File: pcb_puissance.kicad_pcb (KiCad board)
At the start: 2 copper layers, 126.5 x 120.5 mm, 40 parts, among them J1 1755736, J10 Conn_01x02, J11 Conn_01x02, J2 1755736, J3 1755736, J4 1755736, J5 1755736, J6 1755736, J7 1755736, J8 1755736, J9 Conn_01x02, K1 SRD-05VDC-SL-C

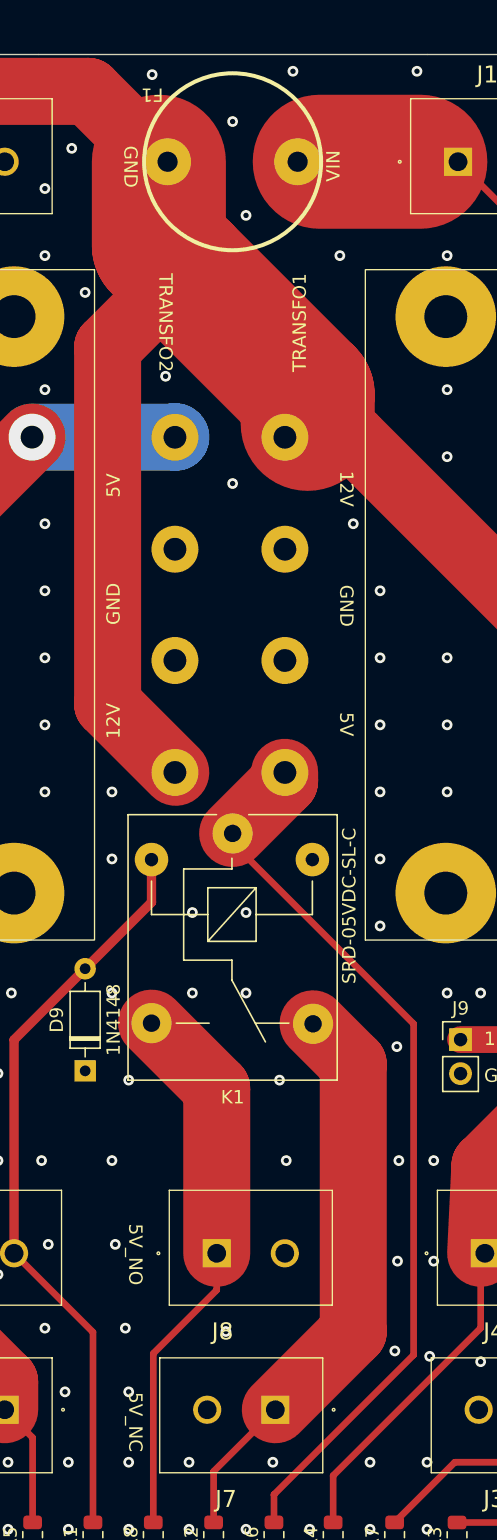
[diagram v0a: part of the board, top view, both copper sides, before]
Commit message: Rectification empreinte relai
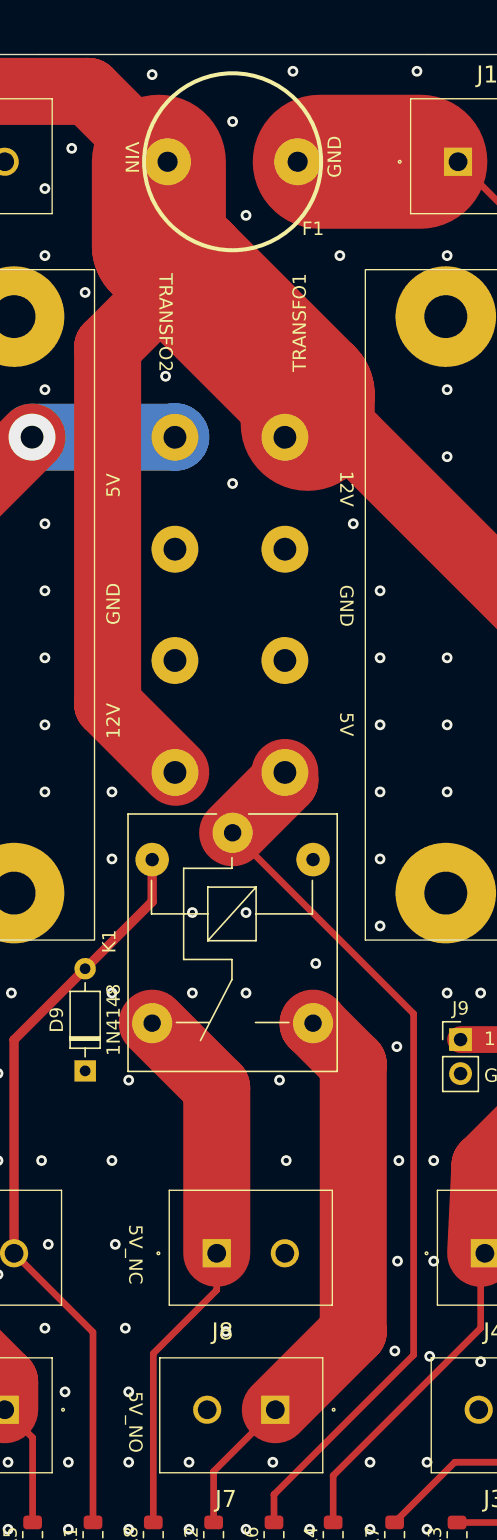
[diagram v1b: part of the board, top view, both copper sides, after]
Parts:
- K1: footprint Relay_THT:Relay_SPDT_SANYOU_SRD_Series_Form_C -> Library:SRD-05VDC-SL-C
- turned F1 to 90 degrees
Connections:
- F1 pad 1: BATTERY -> +12V
- F1 pad 2: +12V -> BATTERY
- K1 pad 1: TRANSFO1 -> GND
- K1 pad 2: BUTTON_NO -> TRANSFO1
- K1 pad 5: GND -> BUTTON_NO
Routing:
- net +12V: track 196.9 -> 194.7 mm
- net GND: vias 297 -> 298

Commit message: Correctifs version 1.2
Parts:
- R2: value 220Ω -> 1.6kΩ
- R3, R4, R7: value 680Ω -> 1.5kΩ
- R5, R6, R8: value 150Ω -> 360Ω
- moved J8 12.5 mm to (87.2, 126.1), turned to 180 degrees
- moved J7 12.4 mm to (82.9, 114.4), turned to 0 degrees
- moved D9 7.52 mm to (73.0, 93.3), turned to -90 degrees
- moved D2 4.58 mm to (78.0, 142.5)
- moved R2 4.58 mm to (78.0, 135.4)
- moved R8 4.42 mm to (82.5, 135.5)
- moved D8 4.42 mm to (82.5, 142.5)
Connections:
- D9 pad 1: GND -> BUTTON_NO
- D9 pad 2: BUTTON_NO -> GND
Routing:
- net RELAY_NO: track 42.8 -> 41.2 mm
- net RELAY_NC: track 41.2 -> 42.8 mm
